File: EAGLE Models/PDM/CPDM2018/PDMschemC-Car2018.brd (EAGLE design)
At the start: 100 x 80 mm, 26 parts

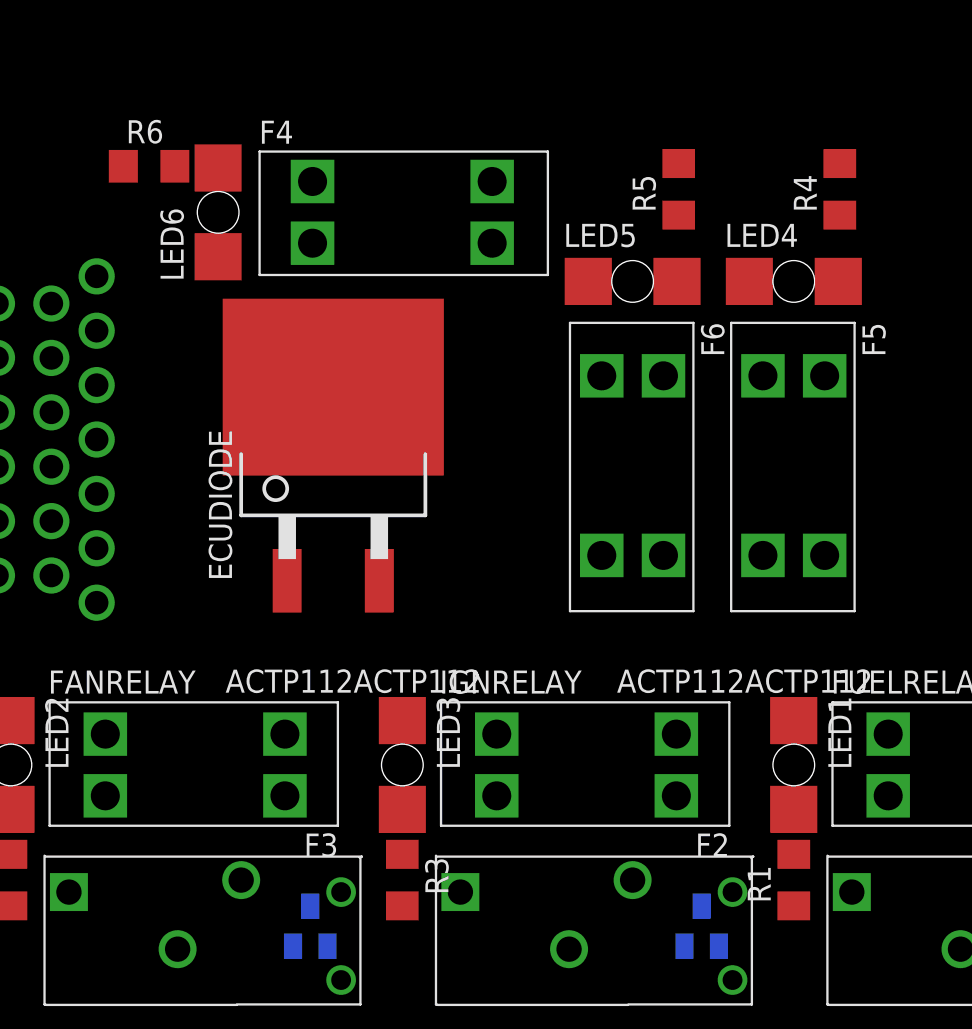
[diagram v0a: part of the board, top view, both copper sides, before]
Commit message: Rearranged resistors and LEDs
Rearranged LEDs and resistors so that the LEDs would be as close as possible to each fuse block.
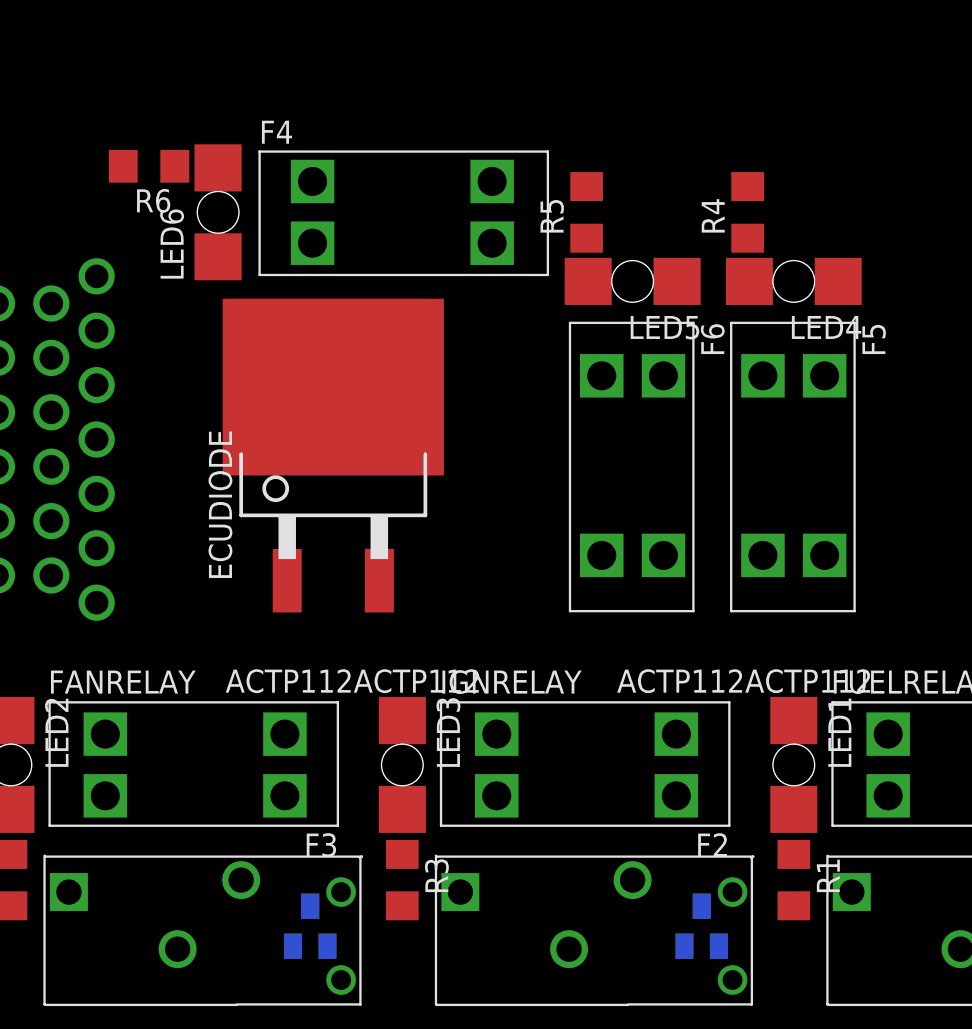
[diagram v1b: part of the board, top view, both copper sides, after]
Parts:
- moved R4 5.24 mm to (55.9, 48.3)
- moved R5 5.24 mm to (47.0, 48.3)
- turned LED4 to 180 degrees
- turned LED5 to 180 degrees
- turned R1 to 270 degrees
- turned R6 to 180 degrees
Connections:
- net DAQ: now also LED4.A; no longer R5.1
- net ECU: now also LED6.A; no longer R6.1
- net GND: now also R1.2, R2.2, R3.2, R4.2, R5.2, R6.2; no longer LED1.C, LED2.C, LED3.C, LED4.C, LED5.C, LED6.C
- net N$1: now also LED2.A; no longer R2.1
- net N$10: now also LED5.C, R5.1; no longer LED5.A, R5.2
- net N$2: now also LED1.C, R1.1; no longer LED1.A, R1.2
- net N$3: now also LED1.A; no longer R1.1
- net N$4: now also LED2.C, R2.1; no longer LED2.A, R2.2
- net N$5: now also LED3.C, R3.1; no longer LED3.A, R3.2
- net N$6: now also LED3.A; no longer R3.1
- net N$7: now also LED4.C, R4.1; no longer LED4.A, R4.2
- net N$8: now also LED6.C, R6.1; no longer LED6.A, R6.2
- net SH/B: now also LED5.A; no longer R4.1

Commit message: Began routing traces
Started creating traces for the PDM. Switched several pins on the connector to help create those traces.
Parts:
- moved FUELRELAY 21.6 mm to (49.5, 11.4)
- moved IGNRELAY 21.6 mm to (71.1, 11.4)
- moved LED1 21.6 mm to (36.8, 17.8)
- moved LED3 21.6 mm to (58.4, 17.8)
- moved R1 21.6 mm to (36.8, 11.4)
- moved R3 21.6 mm to (58.4, 11.4)
- moved U$3 21.6 mm to (74.9, 8.89)
- moved U$4 21.6 mm to (53.3, 8.89)
- moved F1 21.6 mm to (47.0, 17.8)
- moved F2 21.6 mm to (68.6, 17.8)
- turned R2 to 270 degrees
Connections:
- net A23: now also U$1.B19; no longer U$1.B7
- net DAQ: now also U$1.B20, U$1.B21; no longer U$1.B1, U$1.B2
- net ECU: now also U$1.B1, U$1.B2; no longer U$1.B20, U$1.B21
- net FUEL: now also U$1.B13; no longer U$1.B19
- net IGN: now also U$1.B7; no longer U$1.B13
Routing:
- net 12V: track 0.00 -> 6.07 mm
- net N$3: track 0.00 -> 5.52 mm
- net N$6: track 0.00 -> 5.52 mm
- net SH/B: track 0.00 -> 5.52 mm
- net N$1: track 0.00 -> 5.52 mm
- net DAQ: track 0.00 -> 5.52 mm
- net ECU: track 0.00 -> 5.52 mm
- net KILLSW: track 0.00 -> 4.37 mm
- net N$5: track 0.00 -> 2.48 mm
- net N$4: track 0.00 -> 2.48 mm
- net N$2: track 0.00 -> 2.48 mm
- net N$8: track 0.00 -> 2.43 mm
- net N$7: track 0.00 -> 2.43 mm
- net N$10: track 0.00 -> 2.43 mm
- net A23: track 0.00 -> 2.18 mm
- added copper zone on layer 1, net N$11
- added copper zone on layer 1, net N$12
- added copper zone on layer 1, net N$13
- added copper zone on layer 1, net N$14
- added copper zone on layer 1, net N$15
- added copper zone on layer 16, net N$16
- added copper zone on layer 16, net N$17
- added copper zone on layer 16, net N$18
- added copper zone on layer 16, net N$19

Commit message: Finished drawing traces
All of the traces are routed now the board is finished and ready for inspection.
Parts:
- turned U$7 to 90 degrees
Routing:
- net GND: track 0.00 -> 147.4 mm
- net A23: track 2.18 -> 3.47 mm
- added copper zone on layer 16, net N$20
- added copper zone on layer 16, net N$21
- added copper zone on layer 16, net N$22
- added copper zone on layer 16, net N$23
- added copper zone on layer 1, net N$24
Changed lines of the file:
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@@
 <element name="U$3" library="diodes-inc" package="SOT23-3" value="MMBD4448H-7-F" x="74.93" y="8.89" rot="MR0"/>
 <element name="U$4" library="diodes-inc" package="SOT23-3" value="MMBD4448H-7-F" x="53.34" y="8.89" rot="MR0"/>
-<element name="U$7" library="diodes-inc" package="SOT23-3" value="MMBD4448H-7-F" x="31.75" y="8.89" rot="MR0"/>
+<element name="U$7" library="diodes-inc" package="SOT23-3" value="MMBD4448H-7-F" x="31.75" y="8.89" rot="MR90"/>
 <element name="R4" library="resistor" library_urn="urn:adsk.eagle:library:348" package="R1206" package3d_urn="urn:adsk.eagle:package:26062/1" value="" x="55.88" y="48.26" rot="R90"/>
 <element name="LED4" library="led" library_urn="urn:adsk.eagle:library:259" package="P47F-BOTTOM" package3d_urn="urn:adsk.eagle:package:15878/1" value="LAP4-BOTTOM" x="58.42" y="44.45" rot="R180"/>
@@
 <contactref element="ECUDIODE" pad="2"/>
 <contactref element="U$1" pad="B5"/>
-<wire x1="31.75" y1="9.99" x2="32.6722" y2="9.99" width="0.1524" layer="16"/>
+<wire x1="32.85" y1="8.89" x2="32.6722" y2="9.99" width="0.1524" layer="16"/>
 <wire x1="32.6722" y1="9.99" x2="33.4518" y2="10.7696" width="0.1524" layer="16"/>
 <wire x1="74.93" y1="9.99" x2="75.8522" y2="9.99" width="0.1524" layer="16"/>
@@
 <contactref element="R3" pad="2"/>
 <contactref element="R2" pad="2"/>
-<wire x1="46.99" y1="49.682" x2="55.88" y2="49.682" width="0" layer="19" extent="1-1"/>
-<wire x1="21.438" y1="50.8" x2="46.99" y2="49.682" width="0" layer="19" extent="1-1"/>
-<wire x1="17.47" y1="40.23" x2="21.438" y2="50.8" width="0" layer="19" extent="1-1"/>
+<wire x1="16.51" y1="3.81" x2="15.24" y2="5.08" width="0.1524" layer="1"/>
+<wire x1="16.51" y1="3.81" x2="34.29" y2="3.81" width="0.1524" layer="1"/>
+<wire x1="34.29" y1="3.81" x2="36.83" y2="6.35" width="0.1524" layer="1"/>
+<wire x1="34.29" y1="3.81" x2="55.88" y2="3.81" width="0.1524" layer="1"/>
+<wire x1="55.88" y1="3.81" x2="58.42" y2="6.35" width="0.1524" layer="1"/>
+<wire x1="15.24" y1="10.008" x2="12.852" y2="10.008" width="0.1524" layer="1"/>
+<wire x1="12.852" y1="10.008" x2="8.89" y2="13.97" width="0.1524" layer="1"/>
+<wire x1="8.89" y1="13.97" x2="8.89" y2="26.67" width="0.1524" layer="1"/>
+<wire x1="8.89" y1="26.67" x2="11.43" y2="29.21" width="0.1524" layer="1"/>
+<wire x1="11.43" y1="29.21" x2="11.45" y2="29.21" width="0.1524" layer="1"/>
+<wire x1="11.45" y1="29.21" x2="11.97" y2="29.73" width="0.1524" layer="1"/>
+<wire x1="15.24" y1="5.08" x2="15.24" y2="10.008" width="0.1524" layer="1"/>
+<wire x1="36.83" y1="6.35" x2="36.83" y2="10.008" width="0.1524" layer="1"/>
+<wire x1="58.42" y1="6.35" x2="58.42" y2="10.008" width="0.1524" layer="1"/>
+<wire x1="21.438" y1="50.8" x2="11.43" y2="50.8" width="0.1524" layer="1"/>
+<wire x1="11.43" y1="50.8" x2="10.16" y2="49.53" width="0.1524" layer="1"/>
+<wire x1="10.16" y1="40.54" x2="11.97" y2="38.73" width="0.1524" layer="1"/>
+<wire x1="10.16" y1="49.53" x2="10.16" y2="40.54" width="0.1524" layer="1"/>
+<wire x1="46.99" y1="49.682" x2="46.99" y2="52.07" width="0.1524" layer="1"/>
+<wire x1="46.99" y1="52.07" x2="45.72" y2="53.34" width="0.1524" layer="1"/>
+<wire x1="45.72" y1="53.34" x2="23.978" y2="53.34" width="0.1524" layer="1"/>
+<wire x1="23.978" y1="53.34" x2="21.438" y2="50.8" width="0.1524" layer="1"/>
+<wire x1="55.88" y1="49.682" x2="46.99" y2="49.682" width="0.1524" layer="1"/>
 <wire x1="14.47" y1="40.23" x2="17.47" y2="40.23" width="0" layer="19" extent="1-1"/>
 <wire x1="11.97" y1="38.73" x2="14.47" y2="40.23" width="0" layer="19" extent="1-1"/>
@@
 <wire x1="17.47" y1="34.23" x2="14.47" y2="34.23" width="0" layer="19" extent="1-1"/>
 <wire x1="17.47" y1="31.23" x2="14.47" y2="31.23" width="0" layer="19" extent="1-1"/>
-<wire x1="15.24" y1="10.008" x2="11.97" y2="29.73" width="0" layer="19" extent="1-1"/>
-<wire x1="58.42" y1="10.008" x2="15.24" y2="10.008" width="0" layer="19" extent="1-1"/>
-<wire x1="36.83" y1="10.008" x2="58.42" y2="10.008" width="0" layer="19" extent="1-1"/>
 </signal>
 <signal name="DAQ">
@@
 <contactref element="U$7" pad="1"/>
 <contactref element="FANRELAY" pad="COIL1"/>
-<wire x1="32.7" y1="7.79" x2="32.7" y2="6.67" width="0.1524" layer="16"/>
+<wire x1="30.65" y1="7.94" x2="32.7" y2="6.67" width="0.1524" layer="16"/>
 <wire x1="32.7" y1="6.67" x2="33.4518" y2="5.9182" width="0.1524" layer="16"/>
 <contactref element="U$1" pad="B19"/>
-<wire x1="32.7" y1="7.79" x2="14.47" y2="28.23" width="0" layer="19" extent="16-16"/>
+<wire x1="30.65" y1="7.94" x2="14.47" y2="28.23" width="0" layer="19" extent="16-16"/>
 </signal>
 <signal name="N$8">
@@
 <polygon width="0.1524" layer="16">
 <vertex x="11.43" y="27.94"/>
-<vertex x="12.7" y="27.94"/>
-<vertex x="13.97" y="26.67"/>
-<vertex x="13.97" y="10.16"/>
+<vertex x="12.7" y="26.67"/>
+<vertex x="12.7" y="10.16"/>
 <vertex x="15.24" y="8.89"/>
 <vertex x="25.4" y="8.89"/>
@@
 </polygon>
 </signal>
+<signal name="N$20">
+<polygon width="0.1524" layer="16">
+<vertex x="20.32" y="29.21"/>
+<vertex x="19.05" y="30.48"/>
+<vertex x="43.18" y="30.48"/>
+<vertex x="45.72" y="27.94"/>
+<vertex x="74.93" y="27.94"/>
+<vertex x="80.01" y="21.59"/>
+<vertex x="80.01" y="5.08"/>
+<vertex x="78.74" y="3.81"/>
+<vertex x="54.61" y="3.81"/>
+<vertex x="53.34" y="5.08"/>
+<vertex x="53.34" y="6.35"/>
+<vertex x="54.61" y="7.62"/>
+<vertex x="64.77" y="7.62"/>
+<vertex x="66.04" y="6.35"/>
+<vertex x="76.2" y="6.35"/>
+<vertex x="78.74" y="8.89"/>
+<vertex x="78.74" y="20.32"/>
+<vertex x="73.66" y="26.67"/>
+<vertex x="44.45" y="26.67"/>
+<vertex x="41.91" y="29.21"/>
+</polygon>
+</signal>
+<signal name="N$21">
+<polygon width="0.1524" layer="16">
+<vertex x="19.05" y="26.67"/>
+<vertex x="20.32" y="27.94"/>
+<vertex x="41.91" y="27.94"/>
+<vertex x="44.45" y="25.4"/>
+<vertex x="68.58" y="25.4"/>
+<vertex x="69.85" y="24.13"/>
+<vertex x="69.85" y="8.89"/>
+<vertex x="68.58" y="7.62"/>
+<vertex x="67.31" y="7.62"/>
+<vertex x="66.04" y="8.89"/>
+<vertex x="66.04" y="10.16"/>
+<vertex x="67.31" y="11.43"/>
+<vertex x="67.31" y="22.86"/>
+<vertex x="66.04" y="24.13"/>
+<vertex x="43.18" y="24.13"/>
+<vertex x="40.64" y="26.67"/>
+</polygon>
+</signal>
+<signal name="N$22">
+<polygon width="0.1524" layer="16">
+<vertex x="17.78" y="29.21"/>
+<vertex x="17.78" y="25.4"/>
+<vertex x="40.64" y="25.4"/>
+<vertex x="43.18" y="22.86"/>
+<vertex x="46.99" y="22.86"/>
+<vertex x="48.26" y="21.59"/>
+<vertex x="48.26" y="6.35"/>
+<vertex x="46.99" y="5.08"/>
+<vertex x="44.45" y="5.08"/>
+<vertex x="43.18" y="6.35"/>
+<vertex x="43.18" y="8.89"/>
+<vertex x="45.72" y="11.43"/>
+<vertex x="45.72" y="20.32"/>
+<vertex x="44.45" y="21.59"/>
+<vertex x="41.91" y="21.59"/>
+<vertex x="39.37" y="24.13"/>
+<vertex x="17.78" y="24.13"/>
+<vertex x="16.51" y="25.4"/>
+<vertex x="16.51" y="27.94"/>
+</polygon>
+</signal>
+<signal name="N$23">
+<polygon width="0.1524" layer="16">
+<vertex x="15.24" y="29.21"/>
+<vertex x="15.24" y="25.4"/>
+<vertex x="17.78" y="22.86"/>
+<vertex x="25.4" y="22.86"/>
+<vertex x="26.67" y="21.59"/>
+<vertex x="26.67" y="10.16"/>
+<vertex x="29.21" y="8.89"/>
+<vertex x="34.29" y="7.62"/>
+<vertex x="35.56" y="6.35"/>
+<vertex x="35.56" y="5.08"/>
+<vertex x="34.29" y="3.81"/>
+<vertex x="31.75" y="3.81"/>
+<vertex x="24.13" y="11.43"/>
+<vertex x="24.13" y="20.32"/>
+<vertex x="22.86" y="21.59"/>
+<vertex x="16.51" y="21.59"/>
+<vertex x="13.97" y="24.13"/>
+<vertex x="13.97" y="27.94"/>
+</polygon>
+</signal>
+<signal name="N$24">
+<polygon width="0.1524" layer="1">
+<vertex x="11.43" y="39.37"/>
+<vertex x="11.43" y="30.48"/>
+<vertex x="12.7" y="29.21"/>
+<vertex x="13.97" y="29.21"/>
+<vertex x="15.24" y="30.48"/>
+<vertex x="16.51" y="30.48"/>
+<vertex x="17.78" y="31.75"/>
+<vertex x="17.78" y="39.37"/>
+<vertex x="16.51" y="40.64"/>
+<vertex x="13.97" y="40.64"/>
+<vertex x="12.7" y="40.64"/>
+</polygon>
+</signal>

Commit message: Made changes to PDM board
replaced LEDs and Resistors with correct device/package
made ground plane on both layers
named all planes to remove airwires
added resistor values to schem
connected ignition trace to ign relay
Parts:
- LED1, LED2, LED3, LED4, LED5, LED6: value LAP4-BOTTOM -> (none); device led:P47F-BOTTOM -> led:CHIPLED_0805
- R1, R2, R3, R4, R5, R6: device resistor:R1206 -> resistor:R0805
- moved R1 3.81 mm to (36.8, 15.2)
- moved R2 3.81 mm to (15.2, 15.2)
- moved R3 3.81 mm to (58.4, 15.2)
- moved R4 2.84 mm to (57.1, 45.7), turned to 180 degrees
- moved R5 2.84 mm to (48.3, 45.7), turned to 180 degrees
- moved R6 2.84 mm to (25.4, 49.5), turned to 270 degrees
- moved LED4 1.80 mm to (57.1, 43.2), turned to 270 degrees
- moved LED5 1.80 mm to (48.3, 43.2), turned to 270 degrees
- moved LED6 1.80 mm to (27.9, 49.5), turned to 0 degrees
- moved LED1 1.27 mm to (36.8, 19.1), turned to 180 degrees
- moved LED2 1.27 mm to (15.2, 19.1), turned to 180 degrees
- moved LED3 1.27 mm to (58.4, 19.1), turned to 180 degrees
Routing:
- net GND: track 147.4 -> 0.76 mm
- net SH/B: track 5.52 -> 4.19 mm
- net DAQ: track 5.52 -> 4.19 mm
- net KILLSW: track 4.37 -> 5.49 mm
- net ECU: track 5.52 -> 4.55 mm
- net N$5: track 2.48 -> 1.81 mm
- net N$4: track 2.48 -> 1.81 mm
- net N$2: track 2.48 -> 1.81 mm
- added copper zone on layer 1, net 12V
- added copper zone on layer 16, net A23
- added copper zone on layer 16, net DAQ
- added copper zone on layer 16, net ECU
- added copper zone on layer 16, net FAN
- added copper zone on layer 16, net FUEL
- added copper zone on layer 1, net GND
- added copper zone on layer 16, net IGN
- added copper zone on layer 16, net KILLSW
- added copper zone on layer 1, net N$1
- added copper zone on layer 16, net N$12
- added copper zone on layer 1, net N$3
- added copper zone on layer 1, net N$6
- added copper zone on layer 16, net SH/B
- removed copper zone on layer 1, net N$12
- removed copper zone on layer 1, net N$14
- removed copper zone on layer 1, net N$15
- removed copper zone on layer 16, net N$16
- removed copper zone on layer 16, net N$17
- removed copper zone on layer 16, net N$18
- removed copper zone on layer 16, net N$19
- removed copper zone on layer 16, net N$20
- removed copper zone on layer 16, net N$21
- removed copper zone on layer 16, net N$22
- removed copper zone on layer 16, net N$23
- removed copper zone on layer 1, net N$24
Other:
- board size 100 x 80 mm -> 82.5 x 63.5 mm

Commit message: Updated Resistor values
Provided values for resistors in schematic
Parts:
- R1, R2, R3, R4, R5, R6: value (none) -> 1K
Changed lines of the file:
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@@
 <element name="LED2" library="led" library_urn="urn:adsk.eagle:library:259" package="CHIPLED_0805" package3d_urn="urn:adsk.eagle:package:15821/1" value="" x="15.24" y="19.05" rot="R180"/>
 <element name="LED6" library="led" library_urn="urn:adsk.eagle:library:259" package="CHIPLED_0805" package3d_urn="urn:adsk.eagle:package:15821/1" value="" x="27.94" y="49.53"/>
-<element name="R2" library="resistor" library_urn="urn:adsk.eagle:library:348" package="R0805" package3d_urn="urn:adsk.eagle:package:26059/1" value="" x="15.24" y="15.24" rot="R270"/>
-<element name="R6" library="resistor" library_urn="urn:adsk.eagle:library:348" package="R0805" package3d_urn="urn:adsk.eagle:package:26059/1" value="" x="25.4" y="49.53" rot="R270"/>
+<element name="R2" library="resistor" library_urn="urn:adsk.eagle:library:348" package="R0805" package3d_urn="urn:adsk.eagle:package:26059/1" value="1K" x="15.24" y="15.24" rot="R270"/>
+<element name="R6" library="resistor" library_urn="urn:adsk.eagle:library:348" package="R0805" package3d_urn="urn:adsk.eagle:package:26059/1" value="1K" x="25.4" y="49.53" rot="R270"/>
 <element name="U$1" library="TE" package="SUPERSEAL1.0_26POS" value="SUPERSEAL1.0_26POS" x="15.24" y="35.56" rot="R270"/>
 <element name="U$3" library="diodes-inc" package="SOT23-3" value="MMBD4448H-7-F" x="74.93" y="8.89" rot="MR0"/>
 <element name="U$4" library="diodes-inc" package="SOT23-3" value="MMBD4448H-7-F" x="53.34" y="8.89" rot="MR0"/>
 <element name="U$7" library="diodes-inc" package="SOT23-3" value="MMBD4448H-7-F" x="31.75" y="8.89" rot="MR90"/>
-<element name="R4" library="resistor" library_urn="urn:adsk.eagle:library:348" package="R0805" package3d_urn="urn:adsk.eagle:package:26059/1" value="" x="57.15" y="45.72" rot="R180"/>
+<element name="R4" library="resistor" library_urn="urn:adsk.eagle:library:348" package="R0805" package3d_urn="urn:adsk.eagle:package:26059/1" value="1K" x="57.15" y="45.72" rot="R180"/>
 <element name="LED4" library="led" library_urn="urn:adsk.eagle:library:259" package="CHIPLED_0805" package3d_urn="urn:adsk.eagle:package:15821/1" value="" x="57.15" y="43.18" rot="R270"/>
-<element name="R5" library="resistor" library_urn="urn:adsk.eagle:library:348" package="R0805" package3d_urn="urn:adsk.eagle:package:26059/1" value="" x="48.26" y="45.72" rot="R180"/>
+<element name="R5" library="resistor" library_urn="urn:adsk.eagle:library:348" package="R0805" package3d_urn="urn:adsk.eagle:package:26059/1" value="1K" x="48.26" y="45.72" rot="R180"/>
 <element name="LED5" library="led" library_urn="urn:adsk.eagle:library:259" package="CHIPLED_0805" package3d_urn="urn:adsk.eagle:package:15821/1" value="" x="48.26" y="43.18" rot="R270"/>
-<element name="R3" library="resistor" library_urn="urn:adsk.eagle:library:348" package="R0805" package3d_urn="urn:adsk.eagle:package:26059/1" value="" x="58.42" y="15.24" rot="R270"/>
+<element name="R3" library="resistor" library_urn="urn:adsk.eagle:library:348" package="R0805" package3d_urn="urn:adsk.eagle:package:26059/1" value="1K" x="58.42" y="15.24" rot="R270"/>
 <element name="LED3" library="led" library_urn="urn:adsk.eagle:library:259" package="CHIPLED_0805" package3d_urn="urn:adsk.eagle:package:15821/1" value="" x="58.42" y="19.05" rot="R180"/>
-<element name="R1" library="resistor" library_urn="urn:adsk.eagle:library:348" package="R0805" package3d_urn="urn:adsk.eagle:package:26059/1" value="" x="36.83" y="15.24" rot="R270"/>
+<element name="R1" library="resistor" library_urn="urn:adsk.eagle:library:348" package="R0805" package3d_urn="urn:adsk.eagle:package:26059/1" value="1K" x="36.83" y="15.24" rot="R270"/>
 <element name="LED1" library="led" library_urn="urn:adsk.eagle:library:259" package="CHIPLED_0805" package3d_urn="urn:adsk.eagle:package:15821/1" value="" x="36.83" y="19.05" rot="R180"/>
 </elements>
